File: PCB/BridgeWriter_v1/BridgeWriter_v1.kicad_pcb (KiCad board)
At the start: 4 copper layers, 100 x 65 mm, 226 parts, among them J1 USB_B, J10 Barrel_Jack_MountingPin, J11 USB_C_Receptacle_PowerOnly_6P, J12 Conn_01x01, J13 Conn_01x01, J2 RJ45_Bel_SI-60062-F, J24 Conn_01x04, J25 Conn_01x04, J3 Conn_01x05, J4 Conn_01x06, J5 Conn_01x02, J6 Conn_01x04, J7 Conn_01x04, J8 Conn_01x02, J9 Micro_SD_Card_Det2, SW1 SW_Push, SW10 SW_Push, SW2 BOOT_MODE0, SW3 SW_Push, SW4 SW_Push, SW5 SW_Push, SW6 SW_Push, SW7 SW_Push, SW8 BOOT_MODE1, SW9 SW_Push, U1 STM32H723VGTx, U10 TPS1117LV33S, U11 OKL-T/6-W12N-C, U12 PT86-091940LMR, U13 AM8068, U14 AM8068, U15 MCP9700x-ETT, U16 MCP9700x-ETT, U18 USB_Type-C, U19 CH213K, U2 W6300, U20 KIA75S358F, U21 TLP293, U22 CH213K, U23 CH213K, U3 ESP32-C5-WROOM-1, U4 TLP293, U5 MCP2562-E-SN, U6 MCP2562-E-SN, U7 USB3343, U8 TPS1117LV33S, U9 CH221K, Y1 FC2012SN 32.768K-70NNA0KC0, Y2 XRCGB25M000FFS1AR0, Y3 ECS-600-8-36B-CTN-TR

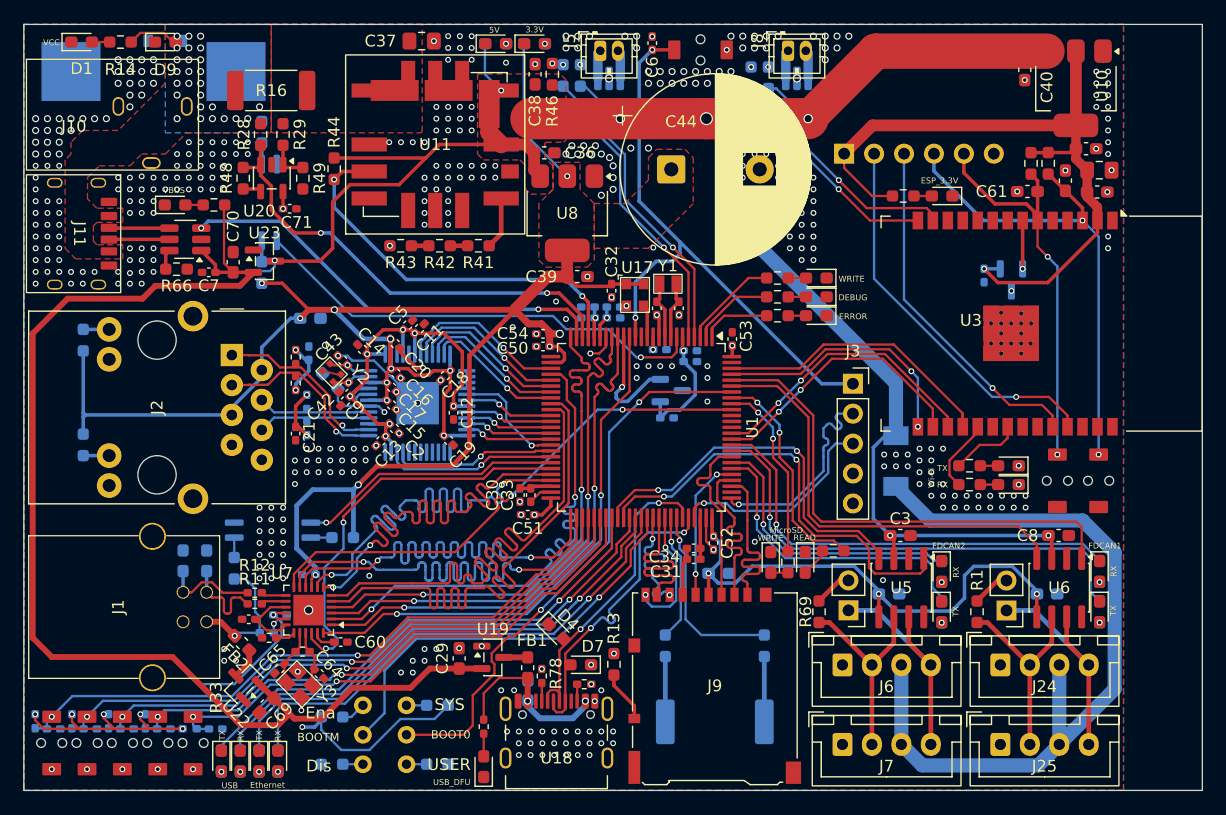
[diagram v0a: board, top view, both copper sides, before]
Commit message: PCB 変更シルクを少しつけた
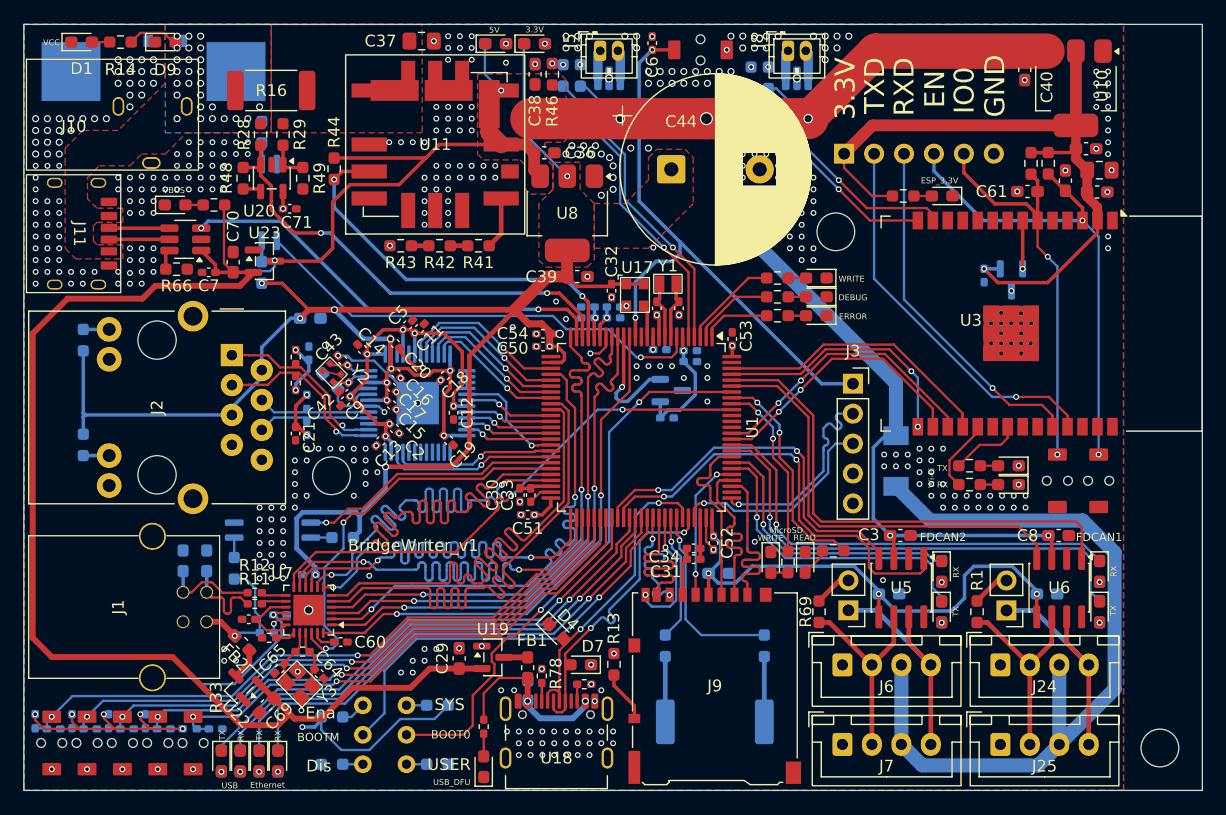
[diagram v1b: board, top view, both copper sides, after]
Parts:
- added H2: MountingHole, MountingHole:MountingHole_3.2mm_M3, F.Cu at (256.4, 121.4)
- added H2: MountingHole, MountingHole:MountingHole_3.2mm_M3, F.Cu at (186.1, 98.3)
- added H2: MountingHole, MountingHole:MountingHole_3.2mm_M3, F.Cu at (228.9, 77.6)
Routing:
- net +3.3V: track 368.5 -> 367.2 mm
- net GND: vias 468 -> 465
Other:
- board text added: "BridgeWriter_v1"
- board text added: "EN"
- board text added: "GND"
- board text added: "IO0"
- board text added: "RXD"
- board text added: "TXD"
